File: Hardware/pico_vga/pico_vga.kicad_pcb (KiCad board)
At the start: 2 copper layers, 80.8 x 60.1 mm, 27 parts, among them J1 Conn_01x40, J2 DB15_Female_HighDensity_Mount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, U1 74HC00, U2 SN74AVC8T245PW, U3 Pico, U4 SN74AVC8T245PW

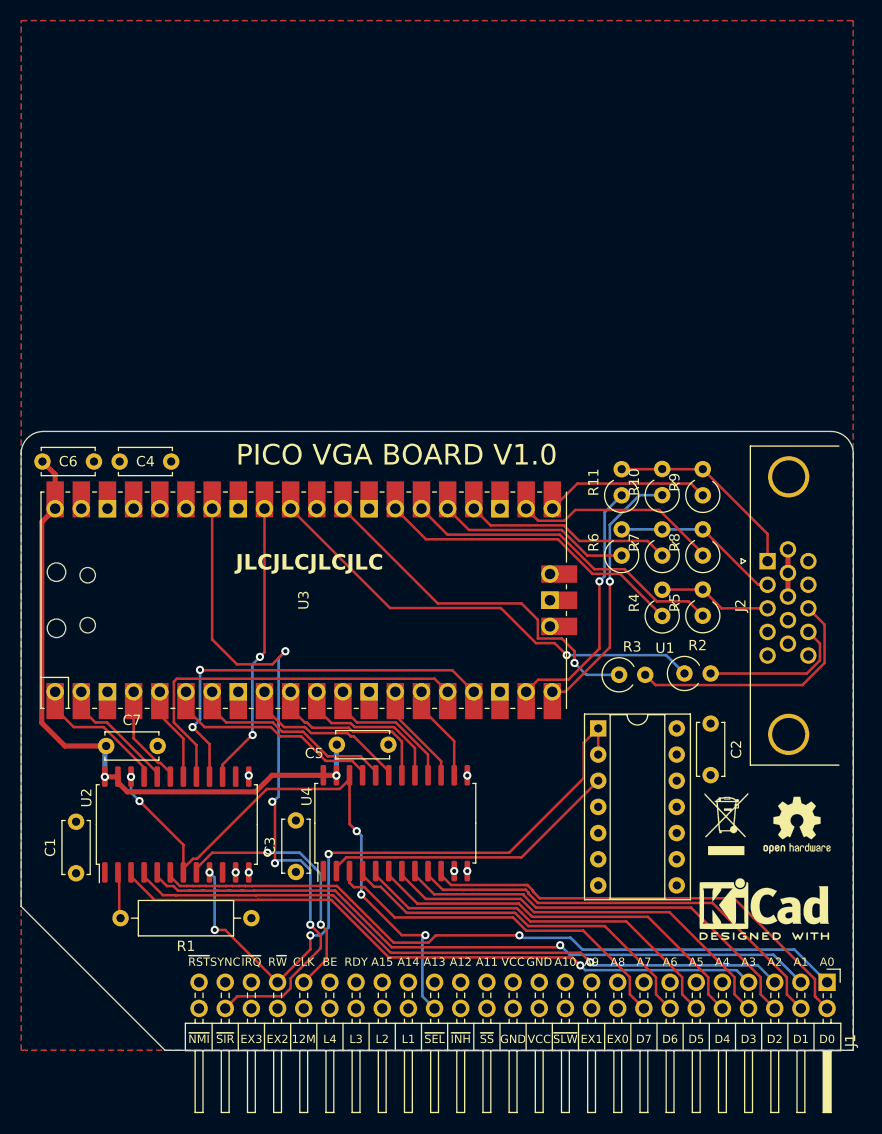
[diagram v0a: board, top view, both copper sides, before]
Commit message: Add RAM board + some VGA things
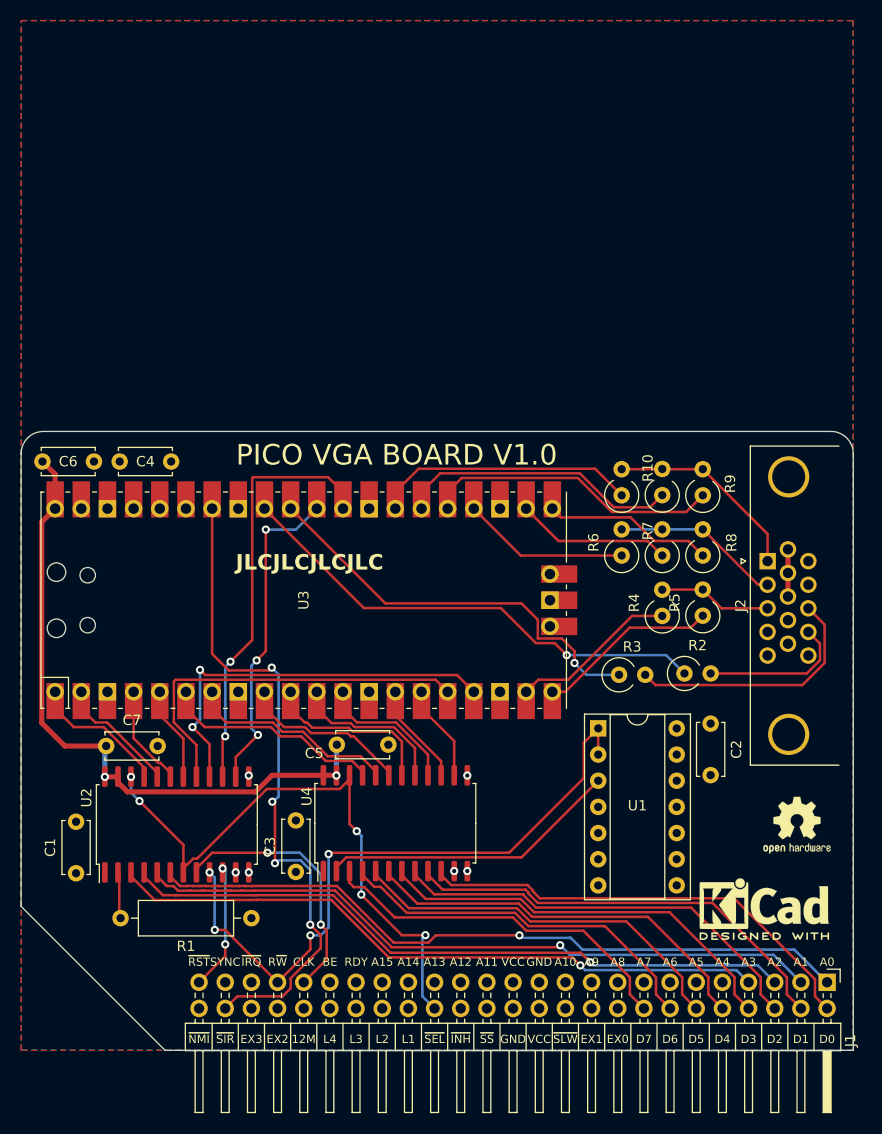
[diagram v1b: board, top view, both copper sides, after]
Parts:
- removed REF**: WEEE-Logo_4.2x6mm_SilkScreen, Symbol:WEEE-Logo_4.2x6mm_SilkScreen
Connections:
- R6 pad 1: /G0 -> /G2
- R8 pad 1: /G2 -> /G0
- U2 pad 10: unconnected-(U2-A8-Pad10) -> ~{RESET}
- U2 pad 14: unconnected-(U2-B8-Pad14) -> /RUN
- U2 pad 15: Net-(U2-B7) -> /RW
- U2 pad 3: A3 -> A0
- U2 pad 4: A2 -> A1
- U2 pad 5: A1 -> A2
- U2 pad 6: A0 -> A3
- U3 pad 19: /R2 -> /B0
- U3 pad 20: /R1 -> /B1
- U3 pad 21: /R0 -> /G0
- U3 pad 22: /G2 -> /G1
- U3 pad 24: /G1 -> /G2
- U3 pad 25: /G0 -> /R0
- U3 pad 26: /B1 -> /R1
- U3 pad 27: /B0 -> /R2
- U3 pad 29: /HSYNC -> /RW
- U3 pad 30: unconnected-(U3-RUN-Pad30) -> /RUN
- U3 pad 31: /VSYNC -> /HSYNC
- U3 pad 32: Net-(U2-B7) -> /VSYNC
- U4 pad 10: D0 -> D7
- U4 pad 3: D7 -> D0
- U4 pad 4: D6 -> D1
- U4 pad 5: D5 -> D2
- U4 pad 6: D4 -> D3
- U4 pad 7: D3 -> D4
- U4 pad 8: D2 -> D5
- U4 pad 9: D1 -> D6
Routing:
- net /RW: track 0.00 -> 41.2 mm, vias 0 -> 2
- net /RUN: track 0.00 -> 31.8 mm, vias 0 -> 3
- net Net-(U2-B7): track 27.7 -> 0.00 mm, vias 2 -> 0
- net /B0: track 30.2 -> 16.3 mm
- net /B1: track 31.6 -> 17.7 mm
- net /R0: track 16.1 -> 29.0 mm
- net ~{RESET}: track 0.00 -> 12.3 mm, vias 0 -> 2
- net /HSYNC: track 35.2 -> 40.3 mm
- net /G1: track 20.2 -> 15.1 mm
- net /G2: track 20.0 -> 16.2 mm
- net /VSYNC: track 44.9 -> 47.4 mm
- net ~{SLOT_IRQ}: track 66.8 -> 64.5 mm
- net /G0: track 18.8 -> 16.7 mm
- net /R1: track 25.5 -> 27.6 mm, vias 1 -> 0
- net /R2: track 24.6 -> 25.6 mm, vias 1 -> 0
